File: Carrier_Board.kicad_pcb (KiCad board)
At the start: 4 copper layers, 190 x 110 mm, 269 parts, among them J10 Conn_01x03_Pin, J11 Conn_01x03_Pin, J12 Conn_01x04_Pin, J13 Conn_01x04_Pin, J14 Conn_01x03_Pin, J15 Bus_M.2_Socket_M, J16 Bus_M.2_Socket_E, J17 Barrel_Jack_Switch, J18 USB_C_Receptacle_USB2.0_16P, J19 Conn_01x04_Pin, J2 Bus_PCI_Express_x4, J20 Conn_01x04_Pin, J21 Conn_01x04_Pin, J3 HDMI_A, J4 USB3_A_Stacked, J5 USB_A_Stacked, J6 RJ45_RB1-125B8G1A, J7 Conn_01x04_Pin, J78 Conn_01x03_Pin, J8 Conn_01x03_Pin, J9 Conn_01x04_Pin, M1 Fan_4pin, M2 Fan_4pin, Q1 2N7002, Q2 2SK3018, Q3 2SK3018, Q4 2SK3018, Q5 2N7002, Q6 2N7002, Q7 AON7262E, Q8 2N7002, SW1 SW_Push, SW2 SW_Push, U1 D3V3XA4B10LP, U10 D3V3XA4B10LP, U11 D3V3XA4B10LP, U12 D3V3XA4B10LP, U13 TL431DBZ, U14 CH224K, U15 LM2734X, U16 LM2734X, U17 D3V3XA4B10LP, U2 D3V3XA4B10LP, U3 D3V3XA4B10LP, U4 D3V3XA4B10LP, U5 D3V3XA4B10LP, U6 RTL8111H-CG-RH, U7 D3V3XA4B10LP, U8 D3V3XA4B10LP, U9 D3V3XA4B10LP, Y1 25MHz

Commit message: Fixed the net labels on U3 and routed them to the USB3 connector with correct impednece matching
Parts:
- removed R15, R18: 2.2k/1%, A_HDJ_Library:R_0402_1005Metric
- added R132: 2.2k/1%, A_HDJ_Library:R_0402_1005Metric, F.Cu at (134.2, 147.9)
- added R134: 2.2k/1%, A_HDJ_Library:R_0402_1005Metric, F.Cu at (134.2, 149.9)
- moved D8 280.4 mm to (109.1, 134.9), turned to 90 degrees
- moved D7 279.3 mm to (111.1, 134.9), turned to 90 degrees
- moved D6 278.3 mm to (113.1, 134.9), turned to 90 degrees
- moved D5 277.3 mm to (115.1, 134.9), turned to 90 degrees
- moved U4 275.6 mm to (112.3, 138.9), turned to -90 degrees
- moved F5 63.7 mm to (59.3, 152.7)
- moved C31 54.7 mm to (63.9, 129.8)
- moved C29 53.3 mm to (64.6, 134.5), turned to -90 degrees
- moved C28 52.2 mm to (65.6, 134.5), turned to -90 degrees
- moved U5 32.0 mm to (74.0, 137.3), turned to 90 degrees
- moved F4 17.5 mm to (59.3, 154.9)
- moved U3 15.6 mm to (64.1, 137.5), turned to -90 degrees
- moved F3 7.31 mm to (119.3, 138.2), turned to -90 degrees
- moved C30 6.31 mm to (118.0, 134.3), turned to 90 degrees
- moved C32 6.17 mm to (75.2, 130.8)
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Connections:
- U3 pad 4: /USB 2.0 & 3.0/CON_USB3_SSRX_N -> /USB 2.0 & 3.0/CON_USB3_SSTX_N
- U3 pad 5: /USB 2.0 & 3.0/CON_USB3_SSRX_P -> /USB 2.0 & 3.0/CON_USB3_SSTX_P
- U3 pad 6: /USB 2.0 & 3.0/CON_USB3_SSRX_P -> /USB 2.0 & 3.0/CON_USB3_SSTX_P
- U3 pad 7: /USB 2.0 & 3.0/CON_USB3_SSRX_N -> /USB 2.0 & 3.0/CON_USB3_SSTX_N
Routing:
- net /USB 2.0 & 3.0/CON_USB3_SSTX_P: track 0.00 -> 13.3 mm, vias 0 -> 1
- net /USB 2.0 & 3.0/CON_USB3_SSTX_N: track 0.00 -> 13.3 mm, vias 0 -> 1
- net /USB 2.0 & 3.0/CON_USB4_SSTX_P: track 0.00 -> 8.68 mm
- net /USB 2.0 & 3.0/CON_USB4_SSTX_N: track 0.00 -> 8.68 mm

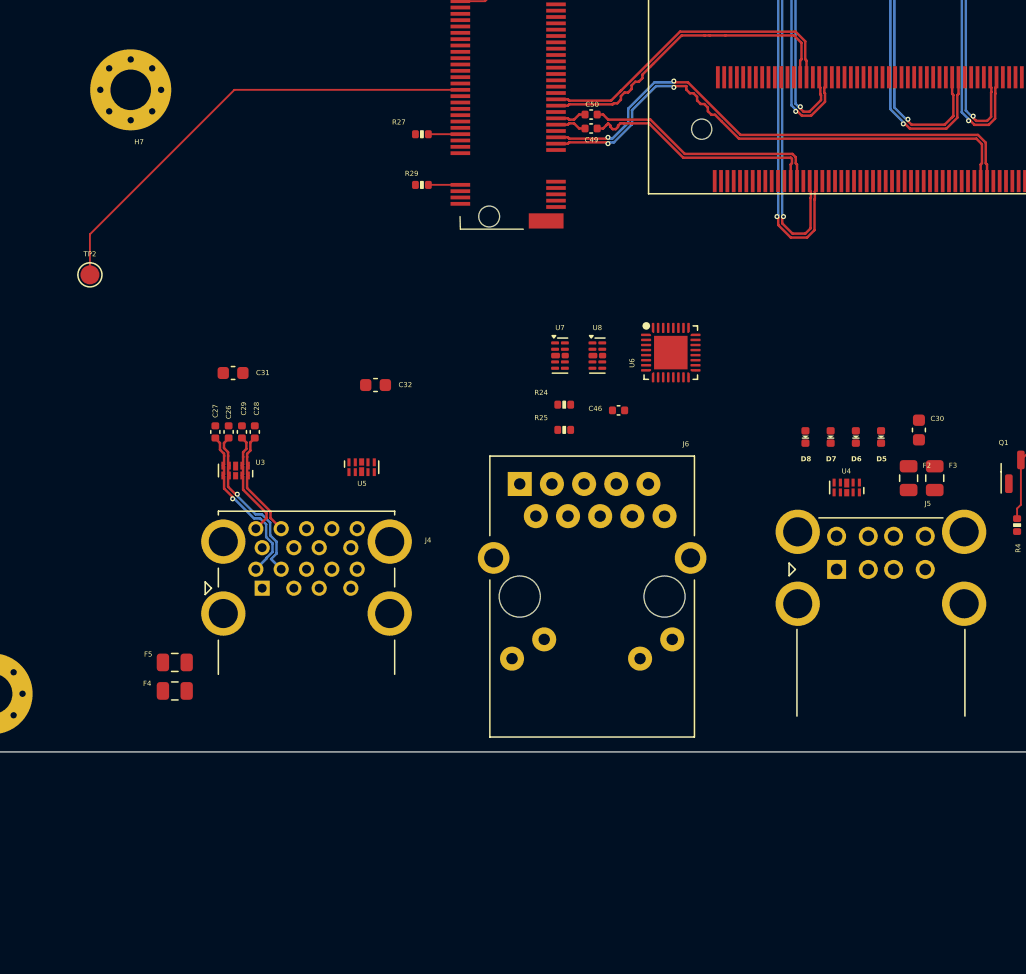
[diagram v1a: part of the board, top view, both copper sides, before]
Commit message: USB 3.0 routed and comleted
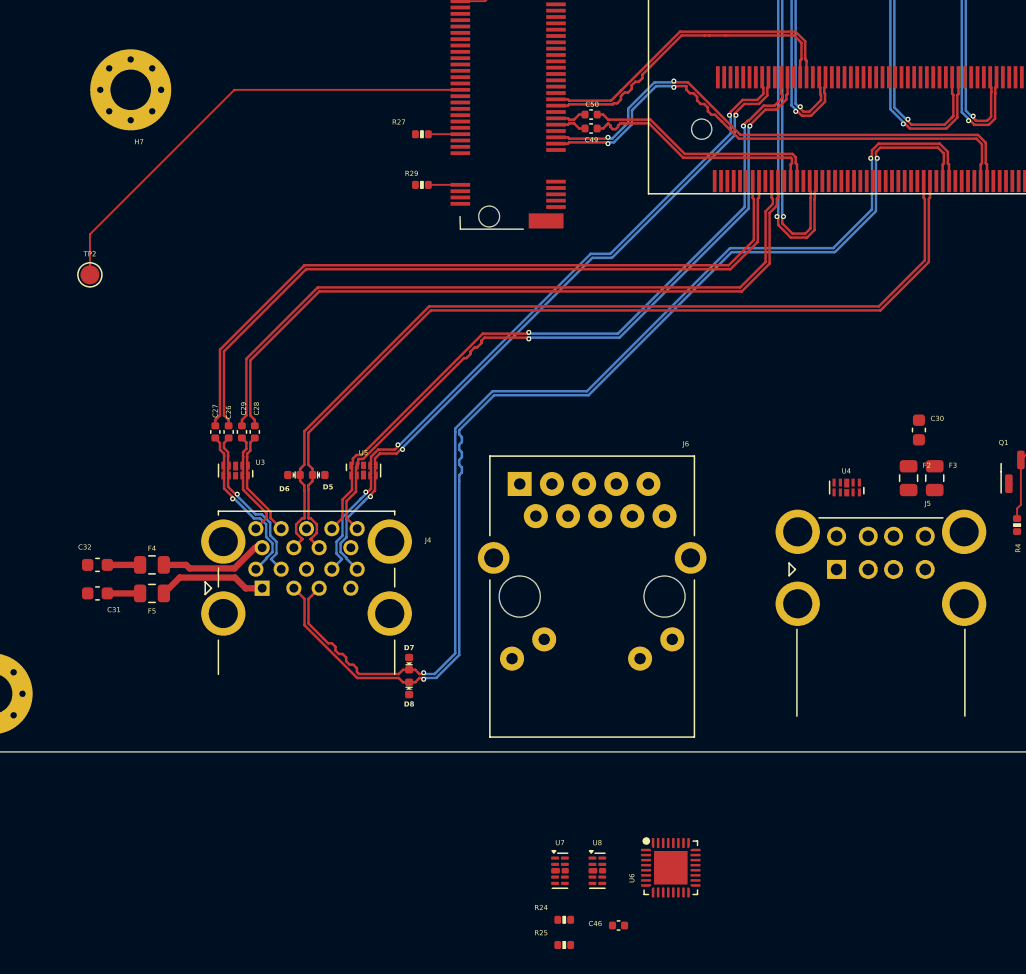
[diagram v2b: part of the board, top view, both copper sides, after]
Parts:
- moved D5 44.5 mm to (70.7, 137.9), turned to 0 degrees
- moved D6 44.5 mm to (68.7, 137.9), turned to 180 degrees
- moved R24 40.7 mm to (90.0, 173.0)
- moved U7 40.7 mm to (89.7, 169.1)
- moved U8 40.7 mm to (92.7, 169.1)
- moved C46 40.7 mm to (94.3, 173.5)
- moved R25 40.7 mm to (90.0, 175.0)
- moved U6 40.7 mm to (98.5, 168.9)
- moved D7 37.8 mm to (77.8, 152.8)
- moved D8 37.1 mm to (77.8, 154.8), turned to -90 degrees
- moved C32 26.1 mm to (53.2, 145.0)
- moved C31 20.4 mm to (53.2, 147.2)
- moved F4 7.91 mm to (57.5, 147.2)
- moved F5 7.91 mm to (57.5, 145.0)
- moved U5 0.30 mm to (74.2, 137.5)
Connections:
- D5 pad 1: /USB 2.0 & 3.0/CON_USB1_D_P -> /USB 2.0 & 3.0/CON_USB4_D_P
- D6 pad 1: /USB 2.0 & 3.0/CON_USB1_D_N -> /USB 2.0 & 3.0/CON_USB4_D_N
- D7 pad 1: /USB 2.0 & 3.0/CON_USB2_D_P -> /USB 2.0 & 3.0/CON_USB3_D_P
- D8 pad 1: /USB 2.0 & 3.0/CON_USB2_D_N -> /USB 2.0 & 3.0/CON_USB3_D_N
- U5 pad 1: /USB 2.0 & 3.0/CON_USB4_SSTX_N -> /USB 2.0 & 3.0/CON_USB4_SSRX_P
- U5 pad 10: /USB 2.0 & 3.0/CON_USB4_SSTX_N -> /USB 2.0 & 3.0/CON_USB4_SSRX_P
- U5 pad 2: /USB 2.0 & 3.0/CON_USB4_SSTX_P -> /USB 2.0 & 3.0/CON_USB4_SSRX_N
- U5 pad 4: /USB 2.0 & 3.0/CON_USB4_SSTX_N -> /USB 2.0 & 3.0/CON_USB3_SSRX_P
- U5 pad 5: /USB 2.0 & 3.0/CON_USB4_SSTX_P -> /USB 2.0 & 3.0/CON_USB3_SSRX_N
- U5 pad 6: /USB 2.0 & 3.0/CON_USB4_SSTX_P -> /USB 2.0 & 3.0/CON_USB3_SSRX_N
- U5 pad 7: /USB 2.0 & 3.0/CON_USB4_SSTX_N -> /USB 2.0 & 3.0/CON_USB3_SSRX_P
- U5 pad 9: /USB 2.0 & 3.0/CON_USB4_SSTX_P -> /USB 2.0 & 3.0/CON_USB4_SSRX_N
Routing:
- net /USB 2.0 & 3.0/CON_USB3_D_P: track 0.00 -> 89.3 mm, vias 0 -> 2
- net /USB 2.0 & 3.0/CON_USB3_D_N: track 0.00 -> 89.3 mm, vias 0 -> 2
- net /USB 2.0 & 3.0/CON_USB4_D_P: track 0.00 -> 71.2 mm
- net /USB 2.0 & 3.0/CON_USB4_D_N: track 0.00 -> 71.2 mm
- net /USB 2.0 & 3.0/CON_USB4_SSRX_N: track 0.00 -> 57.8 mm, vias 0 -> 2
- net /USB 2.0 & 3.0/CON_USB4_SSRX_P: track 0.00 -> 57.7 mm, vias 0 -> 2
- net /LattePanda Module/HSIO_0_TX+: track 0.00 -> 56.6 mm
- net /LattePanda Module/HSIO_0_TX-: track 0.00 -> 56.6 mm
- net /LattePanda Module/HSIO_1_TX-: track 0.00 -> 56.3 mm
- net /LattePanda Module/HSIO_1_TX+: track 0.00 -> 56.3 mm
- net /USB 2.0 & 3.0/CON_USB3_SSRX_N: track 0.00 -> 56.1 mm, vias 0 -> 3
- net /USB 2.0 & 3.0/CON_USB3_SSRX_P: track 0.00 -> 56.1 mm, vias 0 -> 3
- net Net-(J4A-VBUS1): track 0.00 -> 8.64 mm
- net Net-(J4B-VBUS2): track 0.00 -> 8.55 mm
- net +5V: track 0.00 -> 5.17 mm

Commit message: Optimized tracks around Ethernet and repaird the HDMI circuit from component skew memory leak
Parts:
- removed R132, R134: 2.2k/1%, A_HDJ_Library:R_0402_1005Metric
- added R15: 2.2k/1%, A_HDJ_Library:R_0402_1005Metric, F.Cu at (135.8, 141.9)
- added R18: 2.2k/1%, A_HDJ_Library:R_0402_1005Metric, F.Cu at (133.8, 141.9)
- moved C33 305.9 mm to (97.4, 174.7)
- moved C34 305.9 mm to (97.4, 176.6)
- moved C35 305.9 mm to (97.4, 178.6)
- moved C36 305.9 mm to (97.4, 180.6)
- moved C37 305.9 mm to (97.4, 182.5)
- moved C40 305.9 mm to (97.4, 184.5)
- moved C41 305.9 mm to (100.3, 174.7)
- moved C44 305.9 mm to (100.3, 176.6)
- moved C45 305.9 mm to (100.3, 178.6)
- moved C47 305.9 mm to (100.3, 182.5)
- moved R20 305.9 mm to (98.0, 186.7)
- moved R21 305.9 mm to (98.0, 189.2)
- moved R22 305.9 mm to (98.0, 191.8)
- moved R23 305.9 mm to (101.5, 186.5)
- moved Y1 288.2 mm to (92.2, 179.2)
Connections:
- U5 pad 5: /USB 2.0 & 3.0/CON_USB3_SSRX_N -> Net-(U5-NC-Pad6)
- U5 pad 6: /USB 2.0 & 3.0/CON_USB3_SSRX_N -> Net-(U5-NC-Pad6)
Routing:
- net /USB 2.0 & 3.0/CON_USB3_D_P: track 89.3 -> 90.6 mm
- net /USB 2.0 & 3.0/CON_USB3_D_N: track 89.3 -> 90.6 mm

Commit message: Started routing ethernet
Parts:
- moved C123 313.4 mm to (106.0, 133.2), turned to 180 degrees
- moved C124 312.9 mm to (106.0, 131.2), turned to 180 degrees
- moved C125 312.5 mm to (106.0, 129.2), turned to 180 degrees
- moved C126 312.1 mm to (106.0, 127.3), turned to 180 degrees
- moved C131 234.2 mm to (92.2, 161.2)
- moved U6 37.8 mm to (89.8, 132.1), turned to 90 degrees
- moved U8 37.2 mm to (101.9, 133.1)
- moved C46 36.2 mm to (83.0, 139.1), turned to 90 degrees
- moved U7 35.9 mm to (93.8, 133.4)
- moved R23 27.9 mm to (86.4, 163.0)
- moved R25 26.1 mm to (101.2, 151.4), turned to -90 degrees
- moved R24 22.7 mm to (83.2, 151.4), turned to -90 degrees
- moved C47 19.9 mm to (96.3, 163.0)
- moved Y1 15.7 mm to (92.2, 163.6)
- moved C33 8.90 mm to (92.6, 167.2)
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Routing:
- net /Gigabit Ethernet/MDI0+: track 0.00 -> 24.9 mm
- net /Gigabit Ethernet/MDI0-: track 0.00 -> 24.6 mm
- net Net-(J6-PadL3): track 0.00 -> 5.22 mm
- net Net-(J6-CT): track 0.00 -> 3.62 mm
- net Net-(J6-PadL1): track 0.00 -> 2.63 mm

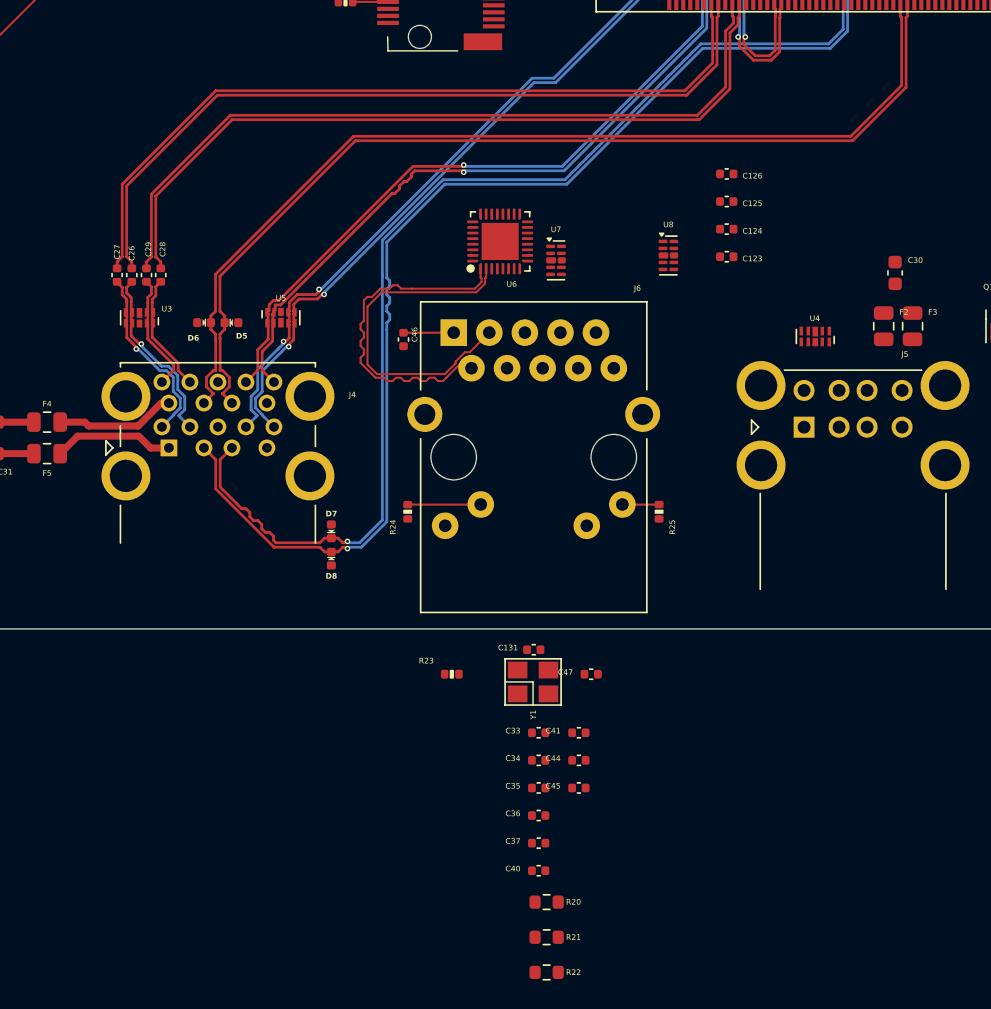
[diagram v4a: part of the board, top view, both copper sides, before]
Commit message: Found and fixed a routing mismatch in the gigabit RX TX pin mis assignment
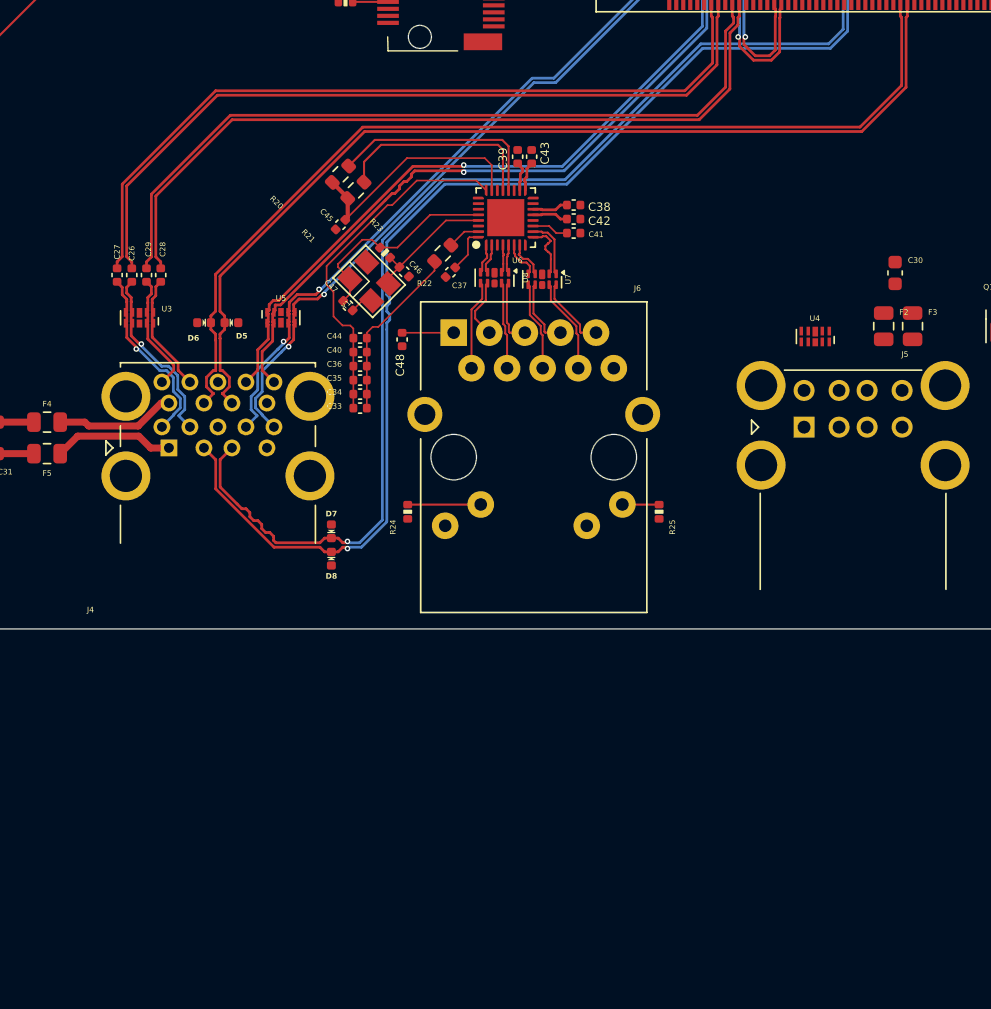
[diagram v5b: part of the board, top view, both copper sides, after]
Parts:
- removed C123, C124, C125, C126: 10uF/50v, A_HDJ_Library:C_0402_1005Metric
- removed C131: 12pF/50V, A_HDJ_Library:C_0402_1005Metric
- added C38: 10uF/50v, A_HDJ_Library:C_0402_1005Metric, F.Cu at (95.1, 129.5)
- added C39: 10uF/50v, A_HDJ_Library:C_0402_1005Metric, F.Cu at (91.1, 126.0)
- added C42: 10uF/50v, A_HDJ_Library:C_0402_1005Metric, F.Cu at (95.1, 130.5)
- added C43: 10uF/50v, A_HDJ_Library:C_0402_1005Metric, F.Cu at (92.1, 126.0)
- added C48: 100nF/50V, A_HDJ_Library:C_0402_1005Metric, F.Cu at (82.8, 139.1)
- C46: value 100nF/50V -> 12pF/50V
- moved R21 55.0 mm to (79.5, 128.4), turned to 45 degrees
- moved R20 54.0 mm to (78.5, 127.3), turned to 45 degrees
- moved R22 51.9 mm to (85.8, 132.9), turned to -135 degrees
- moved C45 43.7 mm to (78.5, 130.9), turned to -135 degrees
- moved C37 41.2 mm to (86.3, 134.3), turned to -135 degrees
- moved C40 39.2 mm to (79.8, 140.0)
- moved C41 35.7 mm to (95.1, 131.5)
- moved C36 34.5 mm to (79.8, 141.0)
- moved C44 34.0 mm to (79.8, 139.0)
- moved C35 31.8 mm to (79.8, 142.0)
- moved C47 31.5 mm to (79.0, 136.7), turned to -45 degrees
- moved Y1 30.9 mm to (80.5, 134.9), turned to -45 degrees
- moved R23 30.5 mm to (81.6, 132.9), turned to -45 degrees
- moved C34 29.1 mm to (79.8, 143.0)
- moved C33 26.5 mm to (79.8, 144.0)
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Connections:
- C46 pad 1: GND -> Net-(U6-CKXTAL2)
- C46 pad 2: Net-(J6-CT) -> GND
- U7 pad 4: /Gigabit Ethernet/MDI2- -> /Gigabit Ethernet/MDI2+
- U7 pad 5: /Gigabit Ethernet/MDI2+ -> /Gigabit Ethernet/MDI2-
- U7 pad 6: /Gigabit Ethernet/MDI2+ -> /Gigabit Ethernet/MDI2-
- U7 pad 7: /Gigabit Ethernet/MDI2- -> /Gigabit Ethernet/MDI2+
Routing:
- net +1V0: track 0.00 -> 25.5 mm
- net +3.3V: track 1.20 -> 24.6 mm
- net /Gigabit Ethernet/MDI0-: track 24.6 -> 6.49 mm
- net /Gigabit Ethernet/MDI0+: track 24.9 -> 8.62 mm
- net Net-(U6-ISOLATEB): track 0.00 -> 15.5 mm
- net Net-(U6-CKXTAL1): track 0.00 -> 15.1 mm
- net Net-(U6-LANWAKEB): track 0.00 -> 14.9 mm
- net GND: track 0.00 -> 14.3 mm
- net /Gigabit Ethernet/MDI3+: track 0.00 -> 11.0 mm
- net /Gigabit Ethernet/MDI3-: track 0.00 -> 9.60 mm
- net /Gigabit Ethernet/MDI2-: track 0.00 -> 9.17 mm
- net Net-(U6-CKXTAL2): track 0.00 -> 9.06 mm
- net /Gigabit Ethernet/MDI1+: track 0.00 -> 8.29 mm
- net /Gigabit Ethernet/MDI2+: track 0.00 -> 7.68 mm
- net /Gigabit Ethernet/MDI1-: track 0.00 -> 6.80 mm
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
